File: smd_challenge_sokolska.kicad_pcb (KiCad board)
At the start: 2 copper layers, 41 x 19.8 mm, 13 parts

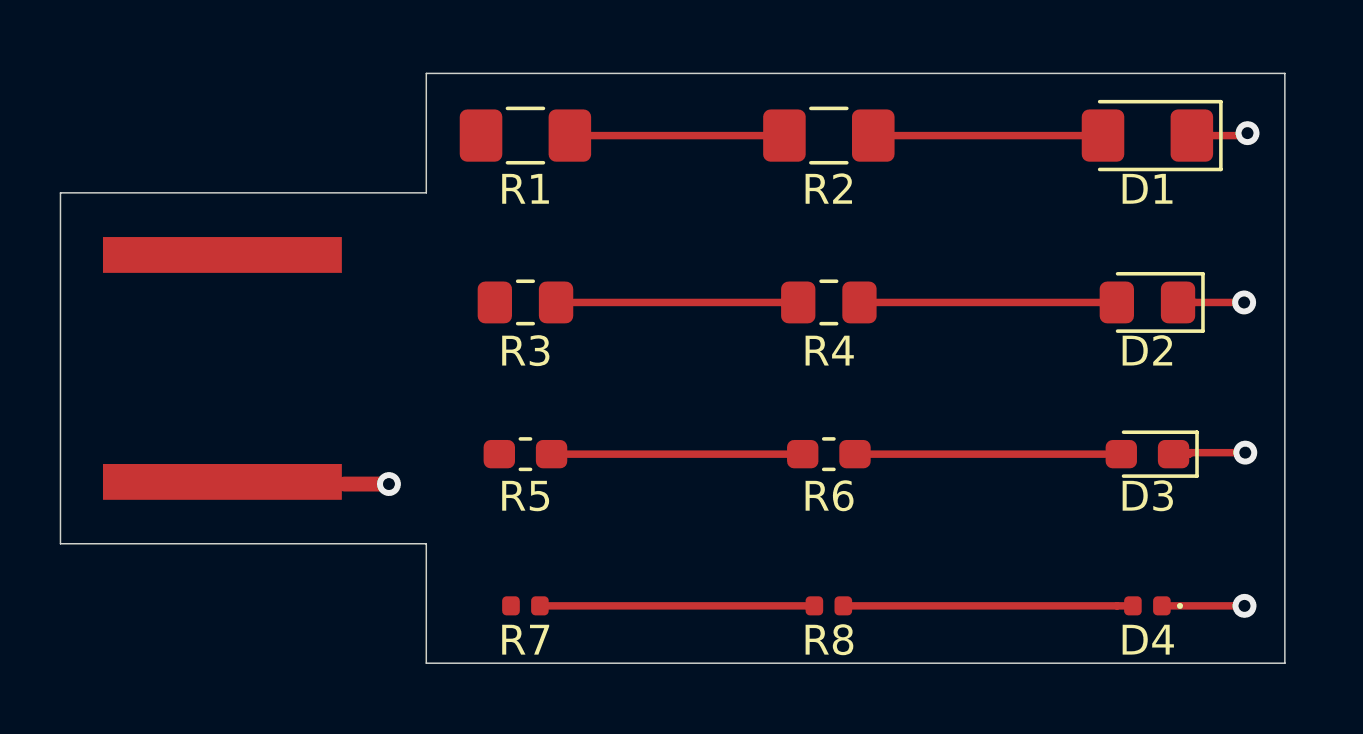
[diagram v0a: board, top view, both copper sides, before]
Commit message: fixed part U01
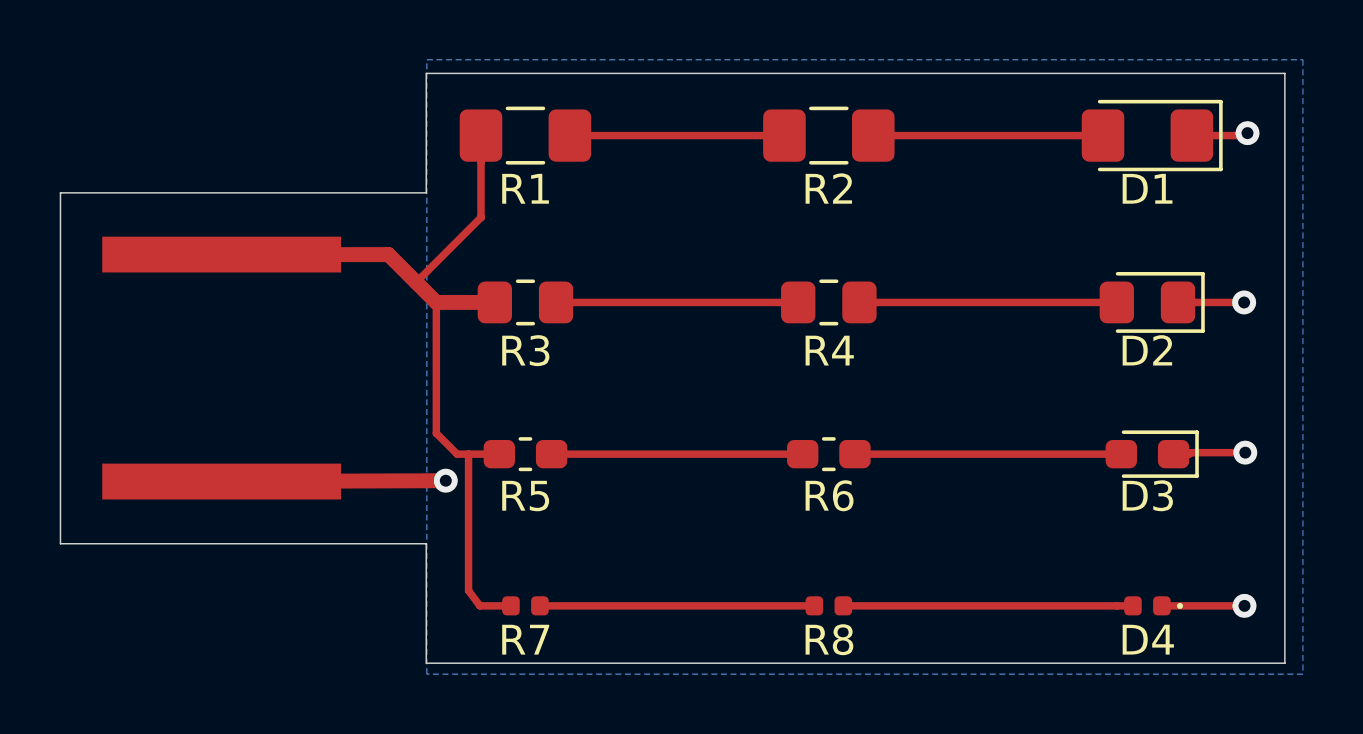
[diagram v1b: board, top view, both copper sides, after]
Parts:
- removed REF**: usb_supply, smd_challenge_sokolska:usb_supply
- added U01: usb_supply, smd_challenge_sokolska:usb_supply, F.Cu at (73.6, 60.6)
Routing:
- net +5V: track 0.00 -> 29.5 mm
- net GND: track 9.30 -> 16.8 mm, vias 4 -> 5
- net (no net): track 1.50 -> 0.00 mm, vias 1 -> 0
- added copper zone on B.Cu, net GND
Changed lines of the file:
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@@
-(kicad_pcb (version 20171130) (host pcbnew "(5.1.5)-3")
+(kicad_pcb (version 20171130) (host pcbnew 5.1.5+dfsg1-2build2)
   (general
     (thickness 1.6)
     (drawings 9)
-    (tracks 23)
+    (tracks 38)
     (zones 0)
     (modules 13)
@@
     (mod_text_size 1 1)
     (mod_text_width 0.15)
-    (pad_size 1.524 1.524)
-    (pad_drill 0.762)
+    (pad_size 8 1.2)
+    (pad_drill 0)
     (pad_to_mask_clearance 0.051)
     (solder_mask_min_width 0.25)
@@
   )
   (module smd_challenge_sokolska:usb_supply (layer F.Cu)
-    (at 73.6727 60.6298)
+    (at 73.6473 60.6171)
     (solder_mask_margin 0.05)
     (clearance 0.2)
-    (attr virtual)
-    (fp_text reference REF** (at -8.2169 -4.8133) (layer F.SilkS) hide
+    (attr smd)
+    (fp_text reference U01 (at -8.2169 -4.8133) (layer F.SilkS) hide
       (effects (font (size 1 1) (thickness 0.15)))
     )
@@
       (effects (font (size 1 1) (thickness 0.15)))
     )
+    (fp_text user "border of USB connector" (at -3.9116 7.8994) (layer Dwgs.User)
+      (effects (font (size 1 1) (thickness 0.15)))
+    )
+    (fp_line (start 6.7 6) (end 6.7 10) (layer Dwgs.User) (width 0.12))
+    (fp_line (start 6.7 -6) (end 6.7 -10) (layer Dwgs.User) (width 0.12))
+    (fp_line (start -5.3 6) (end 6.7 6) (layer Dwgs.User) (width 0.12))
+    (fp_line (start -5.3 -6) (end 6.7 -6) (layer Dwgs.User) (width 0.12))
     (fp_line (start -5.3 6) (end -5.3 -6) (layer Dwgs.User) (width 0.1))
-    (fp_line (start -5.3 -6) (end 6.7 -6) (layer Dwgs.User) (width 0.12))
-    (fp_line (start -5.3 6) (end 6.7 6) (layer Dwgs.User) (width 0.12))
-    (fp_line (start 6.7 -6) (end 6.7 -10) (layer Dwgs.User) (width 0.12))
-    (fp_line (start 6.7 6) (end 6.7 10) (layer Dwgs.User) (width 0.12))
-    (fp_text user "border of USB connector" (at -3.9116 7.8994) (layer Dwgs.User)
-      (effects (font (size 1 1) (thickness 0.15)))
-    )
-    (pad GND smd rect (at 0 3.8) (size 8 1.2) (layers F.Cu F.Paste F.Mask))
-    (pad VCC smd rect (at 0 -3.8) (size 8 1.2) (layers F.Cu F.Paste F.Mask))
+    (pad VCC smd rect (at 0 -3.8) (size 8 1.2) (layers F.Cu F.Paste F.Mask)
+      (net 6 +5V))
+    (pad GND smd rect (at 0 3.8) (size 8 1.2) (layers F.Cu F.Paste F.Mask)
+      (net 2 GND))
   )
   (module Resistor_SMD:R_0402_1005Metric (layer F.Cu)
@@
   (gr_line (start 109.25 50.75) (end 109.25 70.5) (layer Edge.Cuts) (width 0.05))
   (gr_line (start 80.5 50.75) (end 109.25 50.75) (layer Edge.Cuts) (width 0.05))
-  (segment (start 77.75 64.5) (end 79.25 64.5) (width 0.5) (layer F.Cu) (net 0))
-  (via (at 79.25 64.5) (size 0.8) (drill 0.4) (layers F.Cu B.Cu) (net 0))
   (segment (start 95.4675 52.832) (end 103.1605 52.832) (width 0.25) (layer F.Cu) (net 1))
   (via (at 108 52.75) (size 0.8) (drill 0.4) (layers F.Cu B.Cu) (net 2))
@@
   (via (at 107.8992 68.58) (size 0.8) (drill 0.4) (layers F.Cu B.Cu) (net 2))
   (segment (start 105.133 68.58) (end 107.8992 68.58) (width 0.25) (layer F.Cu) (net 2))
+  (segment (start 73.6473 64.4171) (end 81.153 64.389) (width 0.5) (layer F.Cu) (net 2))
+  (via (at 81.153 64.389) (size 0.8) (drill 0.4) (layers F.Cu B.Cu) (net 2))
   (segment (start 95.005 58.42) (end 103.623 58.42) (width 0.25) (layer F.Cu) (net 3))
   (segment (start 94.855 63.5) (end 103.773 63.5) (width 0.25) (layer F.Cu) (net 4))
   (segment (start 94.465 68.58) (end 103.632 68.58) (width 0.25) (layer F.Cu) (net 5))
   (segment (start 103.632 68.58) (end 104.163 68.58) (width 0.25) (layer F.Cu) (net 5))
+  (segment (start 73.6473 56.8171) (end 79.2326 56.8171) (width 0.5) (layer F.Cu) (net 6))
+  (segment (start 80.8355 58.42) (end 82.795 58.42) (width 0.5) (layer F.Cu) (net 6))
+  (segment (start 82.3325 53.707) (end 82.3325 52.832) (width 0.25) (layer F.Cu) (net 6))
+  (segment (start 79.2326 56.8171) (end 79.2326 56.8069) (width 0.25) (layer F.Cu) (net 6))
+  (segment (start 80.1624 57.7469) (end 82.3341 55.5752) (width 0.25) (layer F.Cu) (net 6))
+  (segment (start 79.2326 56.8171) (end 80.1624 57.7469) (width 0.5) (layer F.Cu) (net 6))
+  (segment (start 80.1624 57.7469) (end 80.8355 58.42) (width 0.5) (layer F.Cu) (net 6))
+  (segment (start 82.3325 55.5736) (end 82.3325 52.832) (width 0.25) (layer F.Cu) (net 6))
+  (segment (start 82.3341 55.5752) (end 82.3325 55.5736) (width 0.25) (layer F.Cu) (net 6))
+  (segment (start 80.8355 62.8015) (end 80.8355 58.42) (width 0.25) (layer F.Cu) (net 6))
+  (segment (start 81.534 63.5) (end 80.8355 62.8015) (width 0.25) (layer F.Cu) (net 6))
+  (segment (start 82.945 63.5) (end 81.534 63.5) (width 0.25) (layer F.Cu) (net 6))
+  (segment (start 82.296 68.58) (end 83.335 68.58) (width 0.25) (layer F.Cu) (net 6))
+  (segment (start 81.915 68.072) (end 82.296 68.58) (width 0.25) (layer F.Cu) (net 6))
+  (segment (start 81.915 63.5) (end 81.915 68.072) (width 0.25) (layer F.Cu) (net 6))
   (segment (start 85.3075 52.832) (end 92.4925 52.832) (width 0.25) (layer F.Cu) (net 7))
   (segment (start 84.845 58.42) (end 92.955 58.42) (width 0.25) (layer F.Cu) (net 8))
   (segment (start 84.695 63.5) (end 93.105 63.5) (width 0.25) (layer F.Cu) (net 9))
   (segment (start 84.305 68.58) (end 93.495 68.58) (width 0.25) (layer F.Cu) (net 10))
+  (zone (net 2) (net_name GND) (layer B.Cu) (hatch edge 0.508)
+    (connect_pads (clearance 0.508))
+    (min_thickness 0.254)
+    (fill yes (arc_segments 32) (thermal_gap 0.508) (thermal_bridge_width 0.508))
+    (polygon
+      (pts
+        (xy 109.855 70.866) (xy 80.518 70.866) (xy 80.518 50.292) (xy 109.855 50.292)
+      )
+    )
+  )
 )
